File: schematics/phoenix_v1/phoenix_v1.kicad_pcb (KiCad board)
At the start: 2 copper layers, 106 x 64.5 mm, 15 parts, among them J1 Screw_Terminal_01x02, J2 Conn_01x09_Socket, SW1 RotaryEncoder_Switch, U2 ESP32-S3-DevKitC, U3 NHD-C0220BIZ

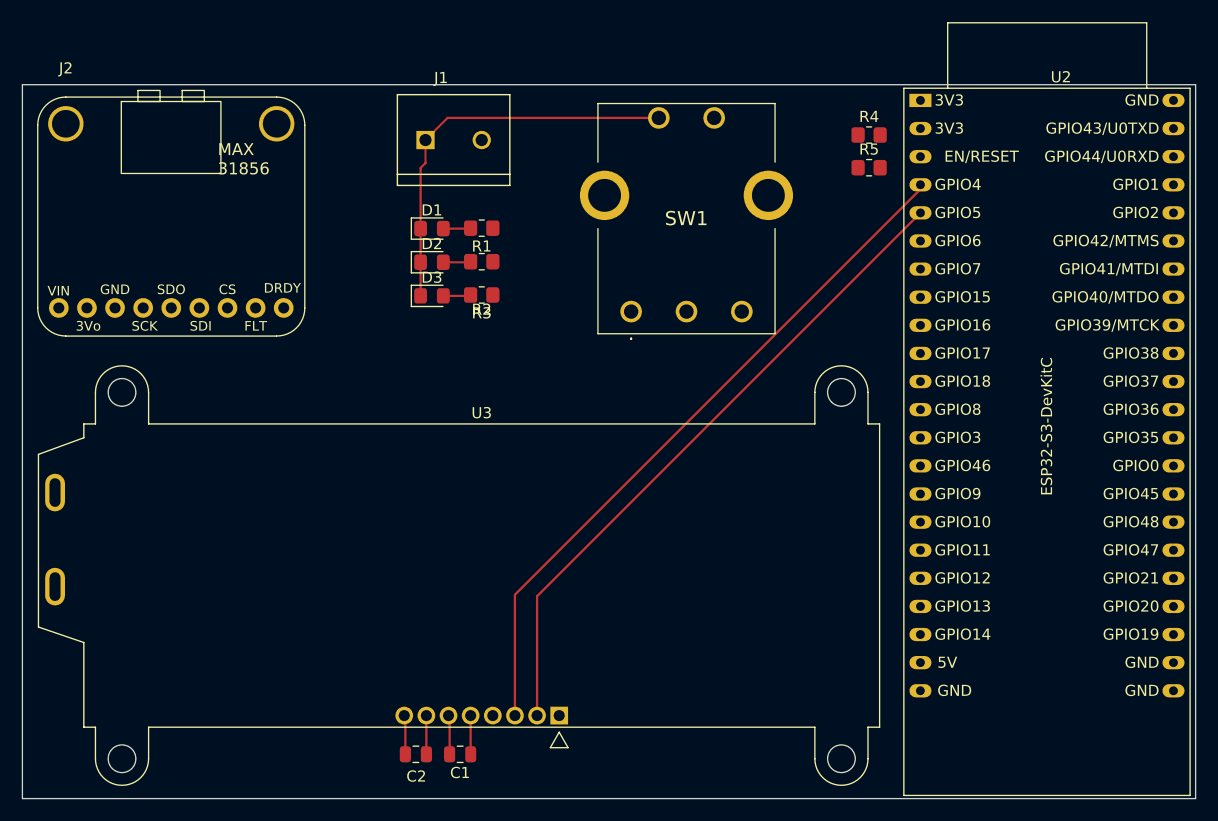
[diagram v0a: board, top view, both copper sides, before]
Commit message: route everything and GND fill and via stitch
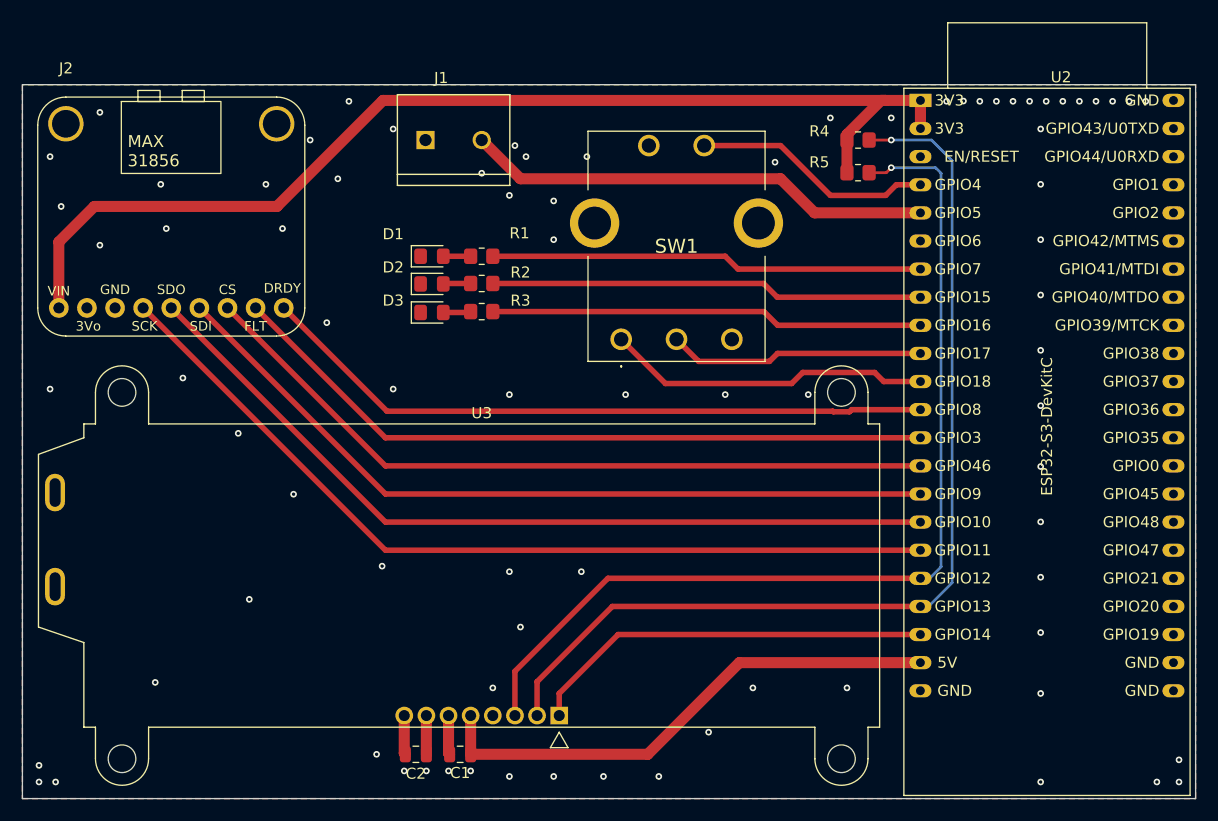
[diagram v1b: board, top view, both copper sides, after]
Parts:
- moved SW1 2.66 mm to (138.1, 81.5)
- moved R1 2.54 mm to (125.5, 74.0)
- moved D1 2.50 mm to (121.0, 74.0)
- moved R2 1.97 mm to (125.5, 76.5)
- moved D2 1.96 mm to (121.0, 76.5)
- moved D3 1.50 mm to (121.0, 79.1)
- moved R3 1.50 mm to (125.5, 79.0)
- moved R4 1.10 mm to (159.5, 63.5)
- moved R5 1.10 mm to (159.5, 66.5)
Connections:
- J2 pad 1: /DRDY -> /MAX_DRDY
- J2 pad 2: /~{FAULT} -> /MAX_FAULT
- J2 pad 3: /~{CS} -> /MAX_CS
- J2 pad 4: /SDI -> /MAX_SDI
- J2 pad 5: /SDO -> /MAX_SDO
- J2 pad 6: /SCK -> /MAX_SCK
- J2 pad 8: +3.3V -> /MAX_3.3VOUT
- J2 pad 9: /VIN_1 -> +3.3V
- R1 pad 1: Net-(U2-GPIO46) -> /LED_1
- R2 pad 1: Net-(U2-GPIO47) -> /LED_2
- R3 pad 1: Net-(U2-GPIO48) -> /LED_3
- U2 pad 10: unconnected-(U2-GPIO17/ADC2_CH6-Pad10) -> /ENC_B
- U2 pad 11: unconnected-(U2-GPIO18/ADC2_CH7-Pad11) -> /ENC_A
- U2 pad 12: unconnected-(U2-GPIO8/ADC1_CH7-Pad12) -> /MAX_DRDY
- U2 pad 13: unconnected-(U2-GPIO3/ADC1_CH2-Pad13) -> /MAX_FAULT
- U2 pad 14: Net-(U2-GPIO46) -> /MAX_CS
- U2 pad 15: unconnected-(U2-GPIO9/ADC1_CH8-Pad15) -> /MAX_SDI
- U2 pad 16: unconnected-(U2-GPIO10/ADC1_CH9-Pad16) -> /MAX_SDO
- U2 pad 17: unconnected-(U2-GPIO11/ADC2_CH0-Pad17) -> /MAX_SCK
- U2 pad 18: unconnected-(U2-GPIO12/ADC2_CH1-Pad18) -> /SDA
- U2 pad 19: unconnected-(U2-GPIO13/ADC2_CH2-Pad19) -> /SCL
- U2 pad 20: unconnected-(U2-GPIO14/ADC2_CH3-Pad20) -> /DISPLAY_RST
- U2 pad 27: SSR_PWM -> unconnected-(U2-GPIO21-Pad27)
- U2 pad 28: Net-(U2-GPIO47) -> unconnected-(U2-GPIO47-Pad28)
- U2 pad 29: Net-(U2-GPIO48) -> unconnected-(U2-GPIO48-Pad29)
- U2 pad 32: /DISPLAY_~{RST} -> unconnected-(U2-GPIO35-Pad32)
- U2 pad 33: /ENC_A -> unconnected-(U2-GPIO36-Pad33)
- U2 pad 34: /ENC_B -> unconnected-(U2-GPIO37-Pad34)
- U2 pad 35: /ENC_SW -> unconnected-(U2-GPIO38-Pad35)
- U2 pad 4: /SDA -> /ENC_SW
- U2 pad 5: /SCL -> SSR_PWM
- U2 pad 7: unconnected-(U2-GPIO7/ADC1_CH6-Pad7) -> /LED_1
- U2 pad 8: unconnected-(U2-GPIO15/ADC2_CH4/32K_P-Pad8) -> /LED_2
- U2 pad 9: unconnected-(U2-GPIO16/ADC2_CH5/32K_N-Pad9) -> /LED_3
- U3 pad 1: /DISPLAY_~{RST} -> /DISPLAY_RST
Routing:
- net +3.3V: track 0.00 -> 99.9 mm
- net /MAX_SCK: track 0.00 -> 79.3 mm
- net /MAX_SDO: track 0.00 -> 75.7 mm
- net /MAX_SDI: track 0.00 -> 72.1 mm
- net /MAX_CS: track 0.00 -> 68.5 mm
- net /MAX_FAULT: track 0.00 -> 64.9 mm
- net /MAX_DRDY: track 0.00 -> 61.5 mm
- net +5V: track 3.50 -> 47.6 mm
- net SSR_PWM: track 0.00 -> 42.4 mm
- net /LED_2: track 0.00 -> 39.2 mm
- net /LED_3: track 0.00 -> 39.2 mm
- net /LED_1: track 0.00 -> 39.1 mm
- net /DISPLAY_RST: track 0.00 -> 36.8 mm
- net GND: track 36.2 -> 0.00 mm, vias 0 -> 82
- net /SCL: track 59.8 -> 90.7 mm, vias 0 -> 1
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- added copper zone on B.Cu, net GND
- added copper zone on F.Cu, net GND
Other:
- board text added: "D1"
- board text added: "D2"
- board text added: "D3"
- board text added: "R1"

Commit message: fix "Dont mix global and local net labels for the same net (SSR_PWM)"
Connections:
- net SSR_PWM renamed /SSR_PWM
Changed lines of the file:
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@@
 	(net 2 "+3.3V")
 	(net 3 "+5V")
-	(net 4 "SSR_PWM")
+	(net 4 "/SSR_PWM")
 	(net 5 "unconnected-(U2-GPIO6{slash}ADC1_CH5-Pad6)")
 	(net 6 "unconnected-(U2-GPIO43{slash}U0TXD-Pad43)")
@@
 			(layers "*.Cu" "*.Mask")
 			(remove_unused_layers no)
-			(net 4 "SSR_PWM")
+			(net 4 "/SSR_PWM")
 			(pinfunction "Pin_2")
 			(pintype "passive")
@@
 			(layers "*.Cu" "*.Mask")
 			(remove_unused_layers no)
-			(net 4 "SSR_PWM")
+			(net 4 "/SSR_PWM")
 			(pinfunction "GPIO5/ADC1_CH4")
 			(pintype "bidirectional")

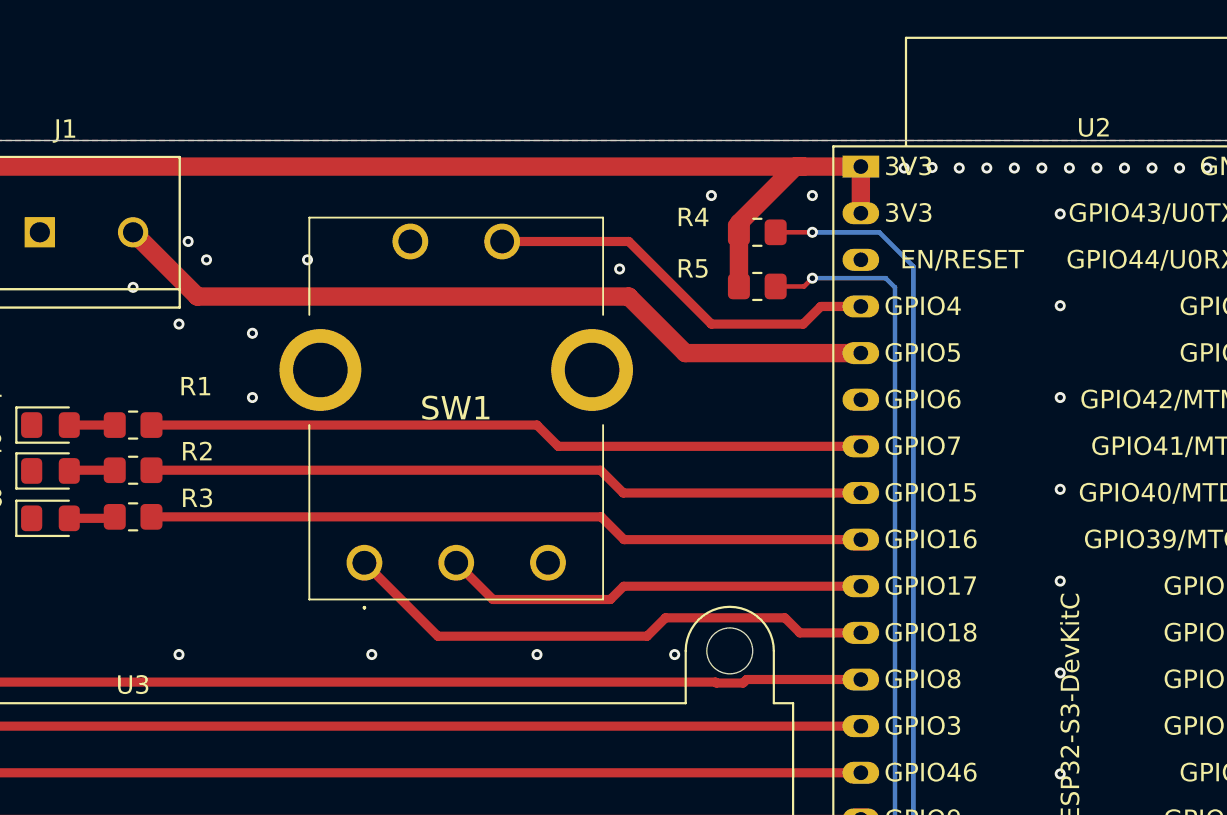
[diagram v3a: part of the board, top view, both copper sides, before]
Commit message: fix "it should be made clear on the schematic that U1 and surrounding components are off board"
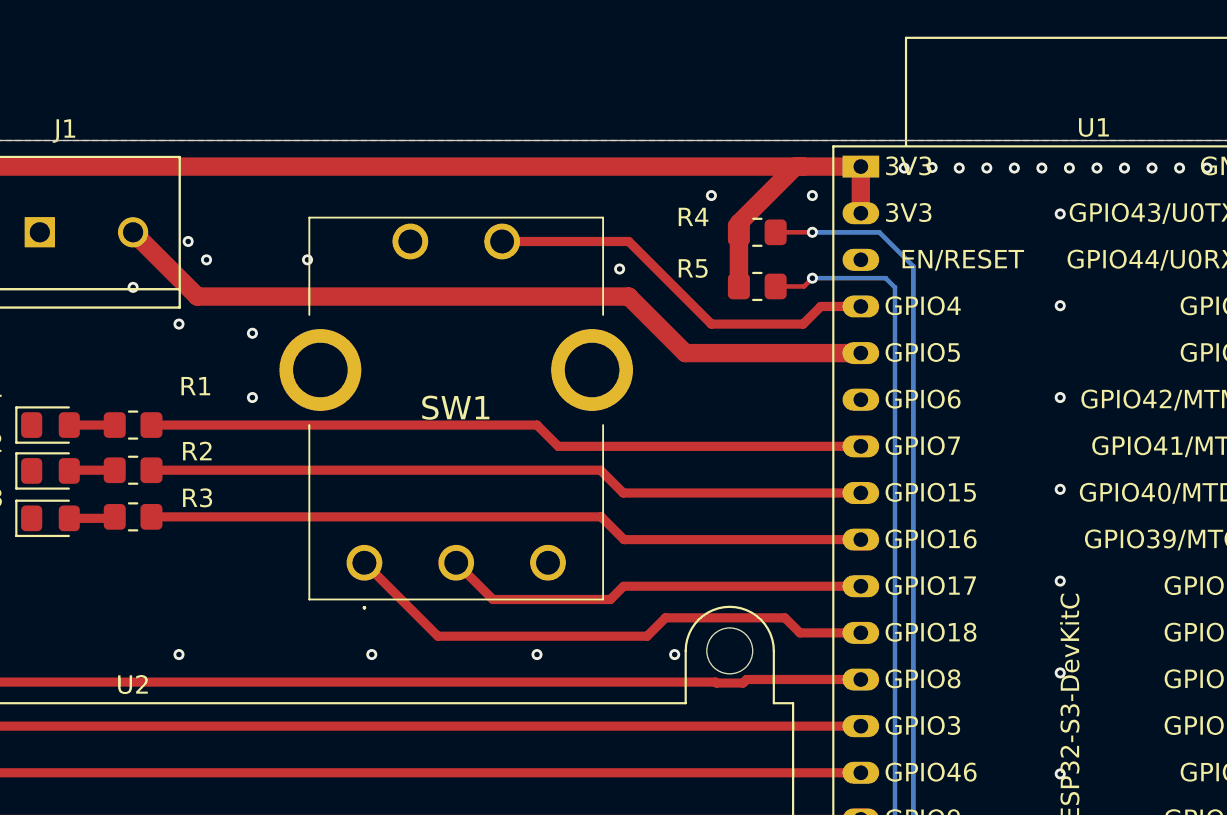
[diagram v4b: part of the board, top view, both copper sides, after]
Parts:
- renumbered U2 to U1, U3 to U2

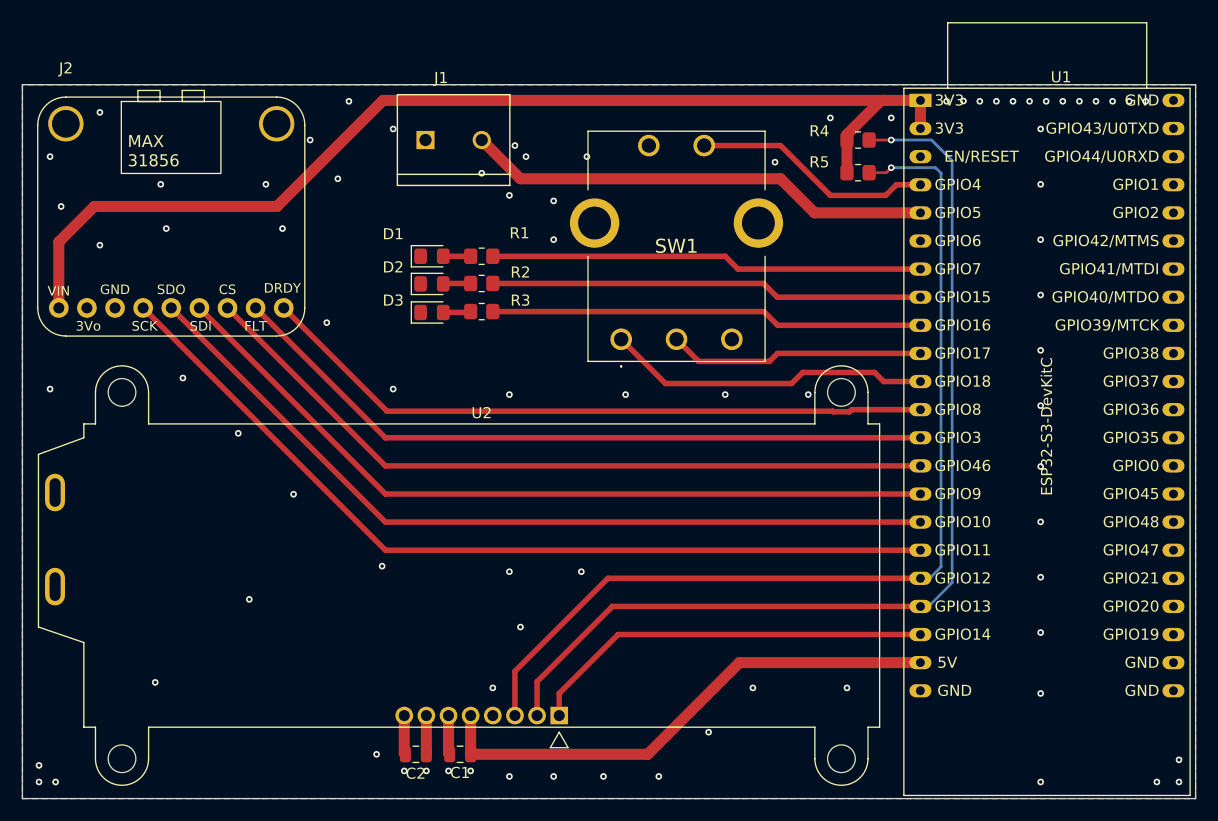
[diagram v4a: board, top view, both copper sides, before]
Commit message: fix "NHD-CO22BIZ needs 3.3V not 5V"
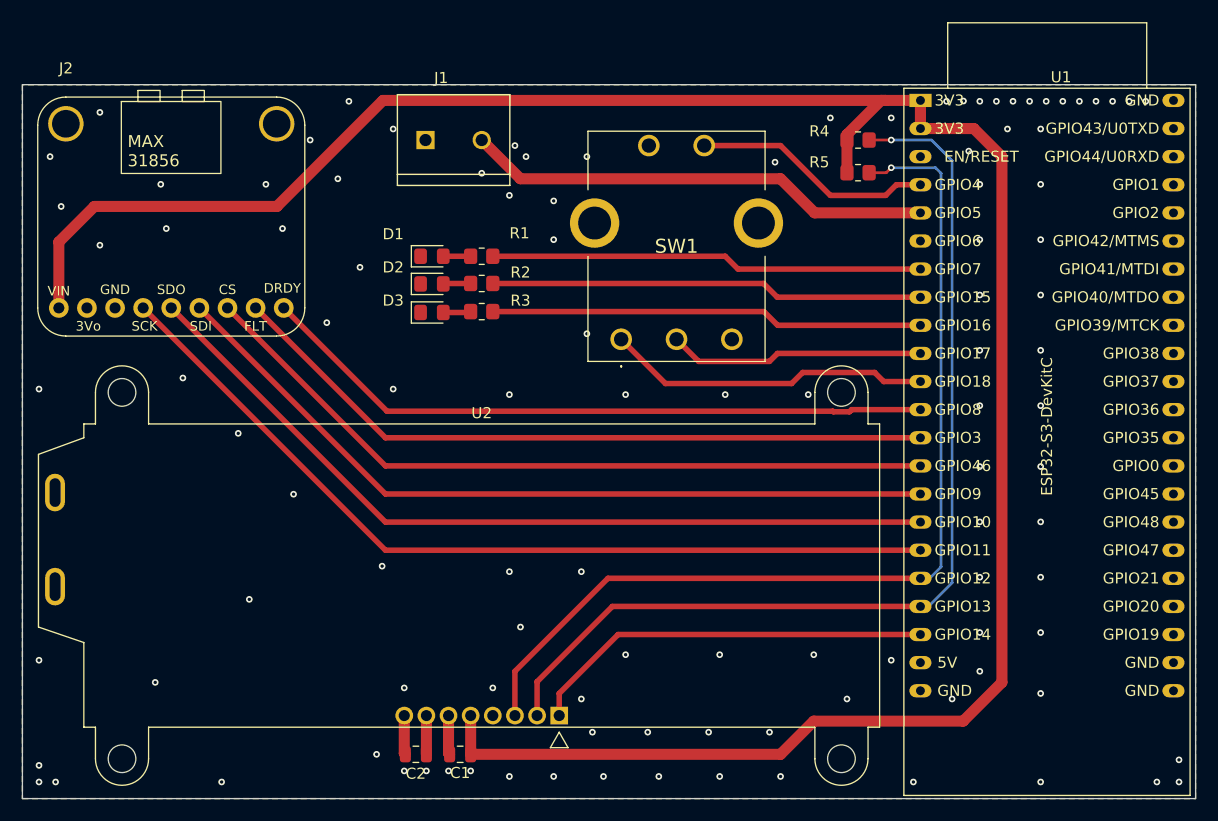
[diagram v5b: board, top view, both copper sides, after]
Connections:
- C1 pad 1: +5V -> +3.3V
- U2 pad 5: +5V -> +3.3V
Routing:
- net +3.3V: track 99.9 -> 210.0 mm
- net +5V: track 47.6 -> 0.00 mm
- net GND: vias 82 -> 110

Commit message: connect A and K on lcd
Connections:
- U2 pad 10: unconnected-(U2-K-Pad10) -> GND
- U2 pad 9: unconnected-(U2-A-Pad9) -> +3.3V
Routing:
- net +3.3V: track 210.0 -> 240.0 mm

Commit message: fix "routing for the I2C pullups VDD trace"
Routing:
- net +3.3V: track 240.0 -> 238.3 mm
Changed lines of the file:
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@@
+	)
+	(segment
+		(start 162 59.92)
+		(end 158.5 59.92)
+		(width 1)
+		(layer "F.Cu")
+		(net 2)
 	)
 	(segment
@@
 	)
 	(segment
-		(start 158.5 63)
-		(end 161.58 59.92)
-		(width 1)
-		(layer "F.Cu")
-		(net 2)
-	)
-	(segment
 		(start 158.5 63.5)
 		(end 158.5 66.45)
@@
 	)
 	(segment
-		(start 162 59.92)
+		(start 158.5 59.92)
 		(end 116.58 59.92)
 		(width 1)
@@
 	(segment
 		(start 158.5 63.5)
-		(end 158.5 63)
+		(end 158.5 59.92)
 		(width 1)
 		(layer "F.Cu")
@@
 		(width 1)
 		(layer "F.Cu")
-		(net 2)
-	)
-	(segment
-		(start 161.58 59.92)
-		(end 162 59.92)
-		(width 1)
-		(layer "F.Cu")

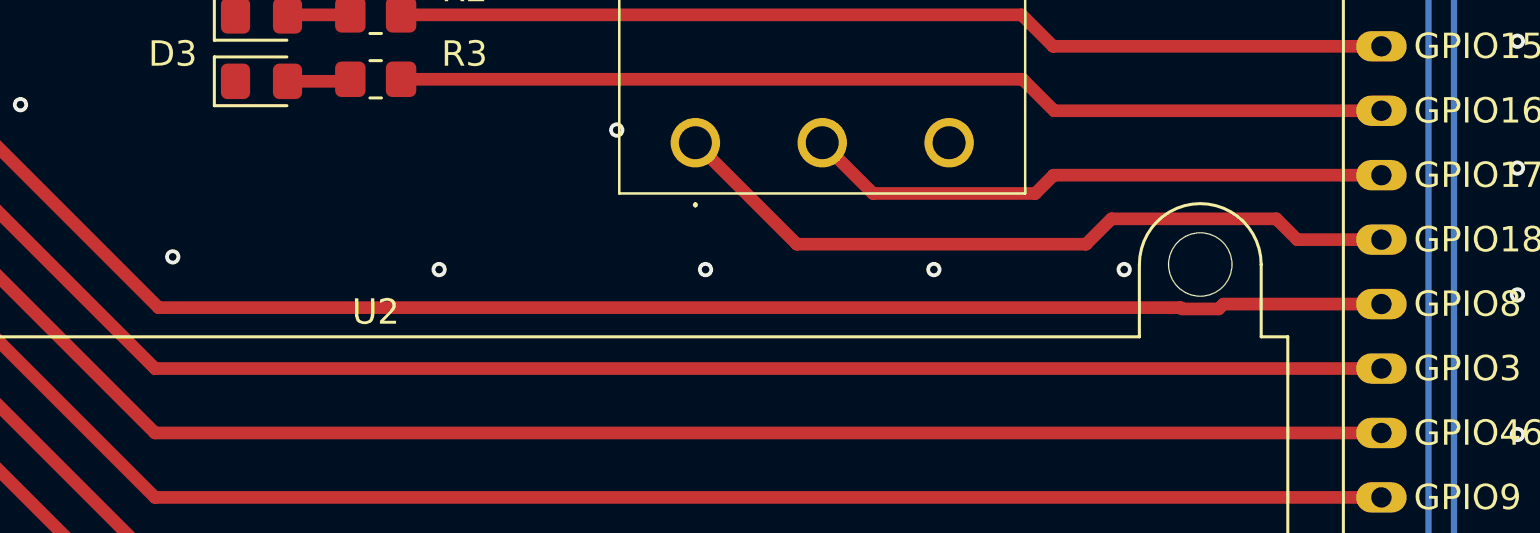
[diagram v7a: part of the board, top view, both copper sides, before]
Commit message: fix "more space on display mounting holes"
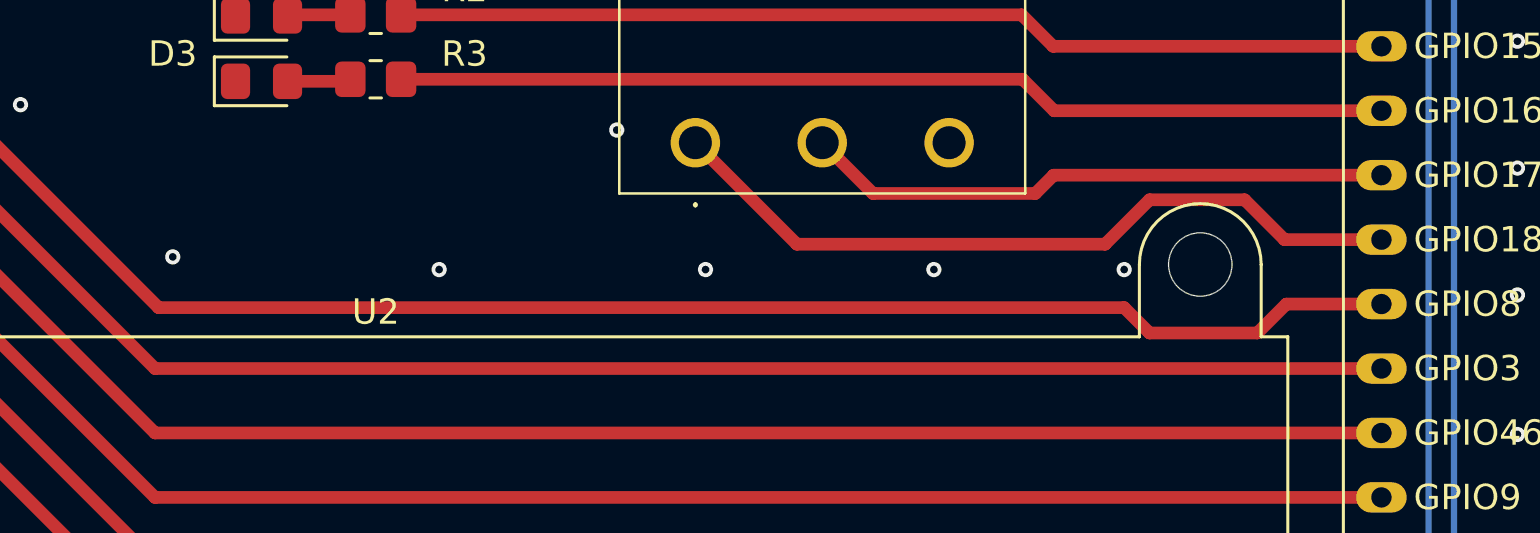
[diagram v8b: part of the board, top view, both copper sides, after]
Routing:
- net /MAX_DRDY: track 61.5 -> 62.3 mm
- net /ENC_A: track 29.5 -> 30.1 mm
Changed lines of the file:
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@@
 	)
 	(segment
-		(start 142.1 85.5)
-		(end 153.5 85.5)
+		(start 161.32 85.32)
+		(end 165.14 85.32)
+		(width 0.5)
+		(layer "F.Cu")
+		(net 14)
+	)
+	(segment
+		(start 156 83.75)
+		(end 159.75 83.75)
+		(width 0.5)
+		(layer "F.Cu")
+		(net 14)
+	)
+	(segment
+		(start 154.25 85.5)
+		(end 156 83.75)
+		(width 0.5)
+		(layer "F.Cu")
+		(net 14)
+	)
+	(segment
+		(start 159.75 83.75)
+		(end 161.32 85.32)
 		(width 0.5)
 		(layer "F.Cu")
@@
 	)
 	(segment
-		(start 161 84.5)
-		(end 161.82 85.32)
-		(width 0.5)
-		(layer "F.Cu")
-		(net 14)
-	)
-	(segment
-		(start 161.82 85.32)
-		(end 165.14 85.32)
-		(width 0.5)
-		(layer "F.Cu")
-		(net 14)
-	)
-	(segment
-		(start 154.5 84.5)
-		(end 161 84.5)
-		(width 0.5)
-		(layer "F.Cu")
-		(net 14)
-	)
-	(segment
-		(start 153.5 85.5)
-		(end 154.5 84.5)
+		(start 142.1 85.5)
+		(end 154.25 85.5)
 		(width 0.5)
 		(layer "F.Cu")
@@
 	)
 	(segment
-		(start 158.725288 88.051)
-		(end 158.776288 88)
+		(start 156 89)
+		(end 160.25 89)
 		(width 0.5)
 		(layer "F.Cu")
@@
 	)
 	(segment
-		(start 158.916288 87.86)
+		(start 155 88)
+		(end 156 89)
+		(width 0.5)
+		(layer "F.Cu")
+		(net 18)
+	)
+	(segment
+		(start 161.39 87.86)
 		(end 165.14 87.86)
 		(width 0.5)
@@
 	)
 	(segment
-		(start 157.274712 88.051)
-		(end 158.725288 88.051)
+		(start 160.25 89)
+		(end 161.39 87.86)
 		(width 0.5)
 		(layer "F.Cu")
@@
 	(segment
 		(start 116.942 88)
-		(end 157.223712 88)
+		(end 155 88)
 		(width 0.5)
 		(layer "F.Cu")
-		(net 18)
-	)
-	(segment
-		(start 157.223712 88)
-		(end 157.274712 88.051)
-		(width 0.5)
-		(layer "F.Cu")
-		(net 18)
-	)
-	(segment
-		(start 158.776288 88)
-		(end 158.916288 87.86)
-		(width 0.5)
-		(layer "F.Cu")
